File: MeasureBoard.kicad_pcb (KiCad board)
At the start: 2 copper layers, 60 x 77 mm, 129 parts, among them J1 Conn_01x04, J10 TEST_1P, J11 TEST_1P, J12 TEST_1P, J13 BARREL_JACK, J14 CONN_01X02, J15 Conn_02x05_Odd_Even, J16 Conn_01x06, J17 GS3, J18 USB_OTG, J19 Conn_01x02, J2 Conn_01x06, J20 Conn_01x02, J21 Conn_01x03, J22 Conn_01x03, J23 Conn_01x03, J24 Conn_01x03, J25 Conn_01x03, J26 Conn_01x03, J27 Conn_02x05_Odd_Even, J3 Conn_01x04, J4 GS3, J5 GS2, J6 Conn_01x04, J7 Conn_01x03, J8 Conn_01x04, J9 TEST_1P, SW1 DIP_SW_2P, SW2 SKRPACE010, SW3 SKRPACE010, SW4 SKRPACE010, U1 L7805, U2 AP1117-33, U3 STM32F103CBTx, U4 NC7SZ08, U5 SP3481CN, U6 NC7WZ241, U7 MCP2562-E-SN, U8 AM26LV32, Y1 Crystal

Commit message: USBのいち変更
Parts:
- moved R19 1.75 mm to (59.5, 93.9), turned to 0 degrees
- moved J18 1.20 mm to (54.0, 92.8)
- moved F1 0.20 mm to (61.0, 90.0)
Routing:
- net GND: track 1161.2 -> 1159.9 mm, vias 267 -> 264
- net Net-(FL1-Pad3): track 32.6 -> 31.4 mm
- net Net-(FL1-Pad1): track 33.3 -> 32.1 mm
- net Net-(F1-Pad2): track 5.19 -> 4.02 mm
- net Net-(D11-Pad2): track 4.52 -> 5.08 mm
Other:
- outline, holes or cut-outs redrawn
- board text added: "v1.1"
- board text removed: "v1.0"

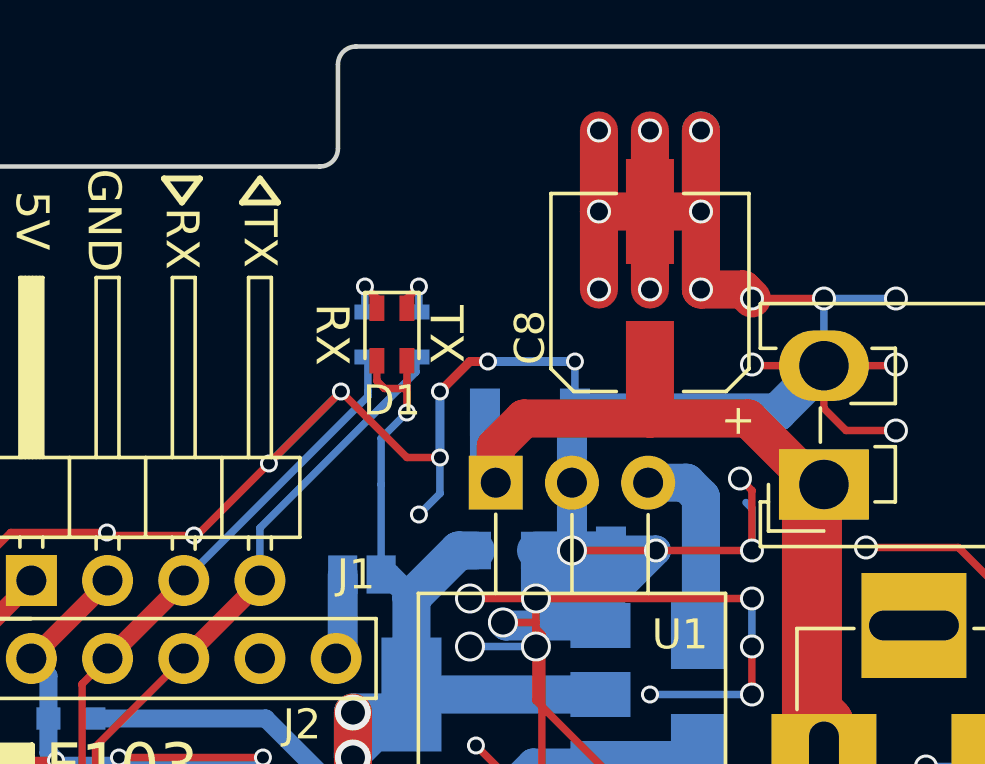
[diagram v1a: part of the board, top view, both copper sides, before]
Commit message: KiCadのバージョンを5.0にアップデート USART3のLEDを調整
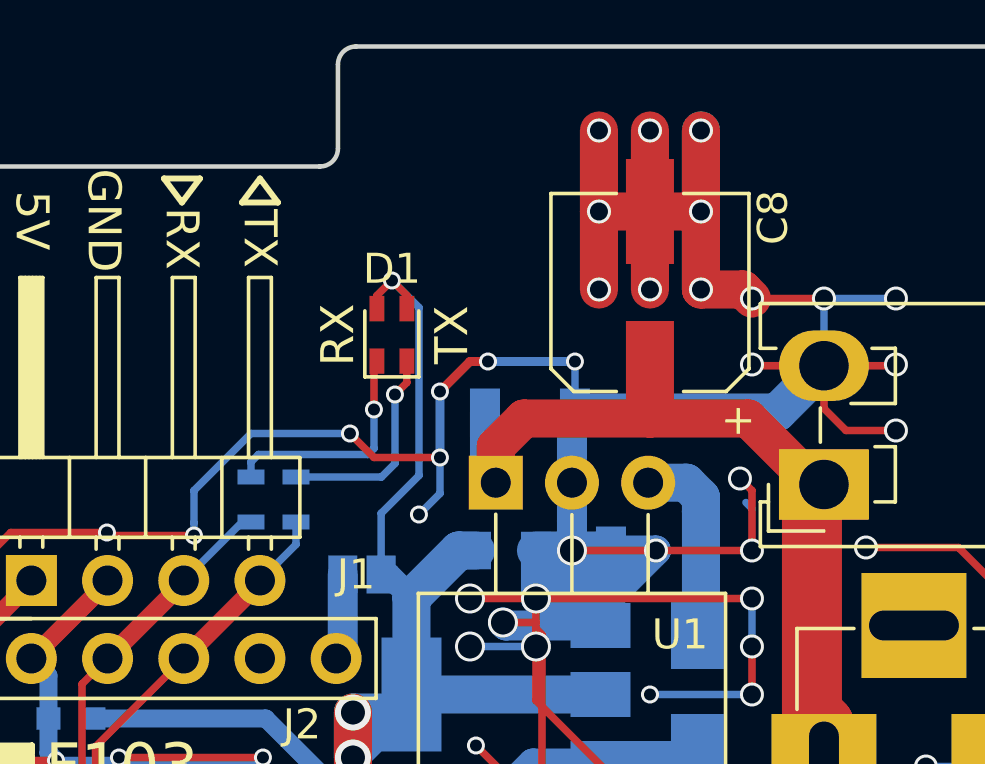
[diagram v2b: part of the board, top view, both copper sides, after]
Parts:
- moved R1 6.80 mm to (78.6, 88.1)
- moved R2 6.74 mm to (77.1, 88.1)
- turned D1 to 90 degrees
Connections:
- R1 pad 2: Net-(D1-Pad2) -> Net-(D1-Pad4)
- R2 pad 2: Net-(D1-Pad4) -> Net-(D1-Pad2)
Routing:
- net /MCU/USART1_TX: track 46.6 -> 39.5 mm
- net /MCU/USART1_RX: track 44.9 -> 38.0 mm
- net Net-(D1-Pad2): track 1.78 -> 7.74 mm
- net Net-(D1-Pad4): track 1.78 -> 7.06 mm
- net +3V3: track 299.2 -> 302.9 mm
- net GND: track 1159.9 -> 1156.4 mm, vias 264 -> 263

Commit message: アノテーションしたけど部品配置がパーになって萎えた
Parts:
- removed C39, C40: 220p, Capacitors_SMD:C_0603
- removed D12: D_TVS, Diodes_SMD:D_SOD-323
- removed J20: Conn_01x02, Pin_Headers:Pin_Header_Straight_2x01_Pitch2.54mm
- removed J21, J22, J23, J24, J25, J26: Conn_01x03, Connectors_JST:JST_EH_B03B-EH-A_03x2.50mm_Straight
- removed J27: Conn_02x05_Odd_Even, Connectors_Multicomp:Multicomp_MC9A12-1034_2x05x2.54mm_Straight
- added JP1: Jumper_2_Open, Jumper:SolderJumper-2_P1.3mm_Open_RoundedPad1.0x1.5mm, F.Cu at (178.5, 73.1)
- added JP2: SolderJumper_3_Open, Jumper:SolderJumper-3_P1.3mm_Open_RoundedPad1.0x1.5mm, F.Cu at (214.6, 84.1)
- added Q1: BSS138, Package_TO_SOT_SMD:SOT-23, F.Cu at (245.7, 84.7)
- added R29: 1.5k, Resistor_SMD:R_0603_1608Metric, F.Cu at (248.9, 85.2)
- added R30: 10k, Resistor_SMD:R_0603_1608Metric, F.Cu at (248.9, 83.7)
- added R31: 36k, Resistor_SMD:R_0603_1608Metric, F.Cu at (241.1, 86.3)
- added R32: R, Resistor_SMD:R_0603_1608Metric, F.Cu at (241.1, 84.8)
- added TP1: TestPoint, MountingHole:MountingHole_3.2mm_M3_Pad, F.Cu at (106.0, 146.0)
- added TP2: TestPoint, MountingHole:MountingHole_3.2mm_M3_Pad, F.Cu at (54.0, 77.0)
- added TP3: TestPoint, MountingHole:MountingHole_3.2mm_M3_Pad, F.Cu at (106.0, 77.0)
- added TP4: TestPoint, MountingHole:MountingHole_3.2mm_M3_Pad, F.Cu at (54.0, 146.0)
- C1, C10, C11, C12, C14, C15, C16, C17, C18, C19, C20, C21, C22, C23, C24, C25, C26, C27, C28, C29, C30, C31, C35, C36, C9: footprint Capacitors_SMD:C_0603 -> Capacitor_SMD:C_0603_1608Metric; moved to F.Cu
- C13: footprint Capacitors_SMD:C_0603 -> Capacitor_SMD:C_0603_1608Metric
- C2, C3: value 0.1u -> C; footprint Capacitors_SMD:C_0603 -> Capacitor_SMD:C_0603_1608Metric; moved to F.Cu
- C32, C33, C34: value 0.1u -> 220p; footprint Capacitors_SMD:C_0603 -> Capacitor_SMD:C_0603_1608Metric; moved to F.Cu
- C37, C38: value 220p -> 0.1u; footprint Capacitors_SMD:C_0603 -> Capacitor_SMD:C_0603_1608Metric; moved to F.Cu
- C4, C6: footprint Capacitors_SMD:C_1206 -> Capacitor_SMD:C_1206_3216Metric; moved to F.Cu
- C5, C7: footprint Capacitors_SMD:C_0805 -> Capacitor_SMD:C_0805_2012Metric; moved to F.Cu
- C8: footprint Capacitors_SMD:CP_Elec_6.3x7.7 -> Capacitor_SMD:CP_Elec_6.3x9.9
- D10: value LED -> D; footprint LEDs:LED_0603 -> Diode_SMD:D_SOD-123F
- D11: value D -> D_TVS; footprint Diodes_SMD:D_SMA -> Diode_SMD:D_SOD-323; moved to F.Cu
- D2: footprint Diodes_SMD:D_SMA -> Diode_SMD:D_SOD-123F; moved to F.Cu
- D3, D4, D5, D9: footprint LEDs:LED_0603 -> LED_SMD:LED_0603_1608Metric
- D7: value D_Zener_Small -> D; footprint Diodes_SMD:D_SOD-323 -> Diode_SMD:D_SOD-123F; moved to F.Cu
- D8: value D -> LED; footprint Diodes_SMD:D_SMA -> LED_SMD:LED_0603_1608Metric; moved to F.Cu
- F1: footprint Fuse_Holders_and_Fuses:Fuse_0679H -> Fuse:Fuse_2816_7142Metric
- J1: footprint Pin_Headers:Pin_Header_Angled_1x04_Pitch2.54mm -> Connector_PinHeader_2.54mm:PinHeader_1x04_P2.54mm_Horizontal
- J10: value TEST_1P -> Conn_01x06; footprint Mounting_Holes:MountingHole_3.2mm_M3_Pad -> Connector_JST:JST_EH_B06B-EH-A_1x06_P2.50mm_Vertical
- J11: value TEST_1P -> USB_B_Micro; footprint Mounting_Holes:MountingHole_3.2mm_M3_Pad -> Connector_USB:USB_Micro-B_Molex-105017-0001
- J12: value TEST_1P -> Conn_01x02; footprint Mounting_Holes:MountingHole_3.2mm_M3_Pad -> Connector_PinHeader_2.54mm:PinHeader_1x02_P2.54mm_Vertical
- J13: value BARREL_JACK -> Conn_01x02; footprint Connectors:BARREL_JACK -> Connector_PinHeader_2.54mm:PinHeader_1x02_P2.54mm_Vertical
- J14: value CONN_01X02 -> Conn_01x03; footprint Connectors_JST:JST_VH_S2P-VH_2x2x3.96mm_Horizontal -> Connector_JST:JST_EH_B03B-EH-A_1x03_P2.50mm_Vertical
- J15: value Conn_02x05_Odd_Even -> Conn_01x03; footprint Pin_Headers:Pin_Header_Straight_2x05_Pitch1.27mm_SMD -> Connector_JST:JST_EH_B03B-EH-A_1x03_P2.50mm_Vertical
- J16: value Conn_01x06 -> Conn_01x03; footprint Connectors_JST:JST_EH_B06B-EH-A_06x2.50mm_Straight -> Connector_JST:JST_EH_B03B-EH-A_1x03_P2.50mm_Vertical
- J17: value GS3 -> Conn_02x05_Odd_Even; footprint Connectors:GS3 -> Connector_Multicomp:Multicomp_MC9A12-1034_2x05_P2.54mm_Vertical; moved to F.Cu
- J18: value USB_OTG -> Conn_01x03; footprint Connectors:USB_Micro-B -> Connector_JST:JST_EH_B03B-EH-A_1x03_P2.50mm_Vertical
- J19: value Conn_01x02 -> Conn_01x03; footprint Pin_Headers:Pin_Header_Straight_1x02_Pitch2.54mm -> Connector_JST:JST_EH_B03B-EH-A_1x03_P2.50mm_Vertical
- J2: footprint Pin_Headers:Pin_Header_Straight_1x06_Pitch2.54mm -> Connector_PinHeader_2.54mm:PinHeader_1x06_P2.54mm_Vertical
- J3: footprint Connectors_JST:JST_EH_B04B-EH-A_04x2.50mm_Straight -> Connector_JST:JST_EH_S04B-EH_1x04_P2.50mm_Horizontal
- J4: value GS3 -> Conn_01x04; footprint Connectors:GS3 -> Connector_JST:JST_EH_B04B-EH-A_1x04_P2.50mm_Vertical; moved to F.Cu
- J5: value GS2 -> Conn_01x03; footprint Connectors:GS2 -> Connector_JST:JST_EH_S03B-EH_1x03_P2.50mm_Horizontal; moved to F.Cu
- J6: footprint Connectors_JST:JST_EH_B04B-EH-A_04x2.50mm_Straight -> Connector_JST:JST_EH_B04B-EH-A_1x04_P2.50mm_Vertical
- J7: value Conn_01x03 -> Barrel_Jack_Switch; footprint Connectors_JST:JST_EH_B03B-EH-A_03x2.50mm_Straight -> Connector_BarrelJack:BarrelJack_Horizontal
- J8: value Conn_01x04 -> Conn_01x02; footprint Connectors_JST:JST_EH_B04B-EH-A_04x2.50mm_Straight -> Connector_JST:JST_VH_B2PS-VH_1x02_P3.96mm_Horizontal
- J9: value TEST_1P -> Conn_02x05_Odd_Even; footprint Mounting_Holes:MountingHole_3.2mm_M3_Pad -> Connector_PinHeader_1.27mm:PinHeader_2x05_P1.27mm_Vertical_SMD
- L1: footprint Capacitors_SMD:C_0603 -> Inductor_SMD:L_0603_1608Metric; moved to F.Cu
- R1, R14, R15, R16, R17, R2, R20, R21, R22, R23, R24, R25, R26, R27, R28, R3, R4, R5, R8, R9: footprint Resistors_SMD:R_0603 -> Resistor_SMD:R_0603_1608Metric; moved to F.Cu
- R10, R11, R12, R13, R6, R7: value 4.7k -> 4k7; footprint Resistors_SMD:R_0603 -> Resistor_SMD:R_0603_1608Metric; moved to F.Cu
- R18: footprint Resistors_SMD:R_0603 -> Resistor_SMD:R_0603_1608Metric
- R19: value 100k -> R; footprint Resistors_SMD:R_0603 -> Resistor_SMD:R_0603_1608Metric
- RN1, RN5: value 10k_4 -> R_Pack04; footprint Resistors_SMD:R_Array_Concave_4x0603 -> Resistor_SMD:R_Array_Concave_4x0603
- RN2: value 150_4 -> R_Pack04; footprint Resistors_SMD:R_Array_Concave_4x0603 -> Resistor_SMD:R_Array_Concave_4x0603
- RN3, RN4: value 150_4 -> R_Pack04; footprint Resistors_SMD:R_Array_Concave_4x0603 -> Resistor_SMD:R_Array_Concave_4x0603; moved to F.Cu
- RN6: value 20k_4 -> R_Pack02; footprint Resistors_SMD:R_Array_Concave_4x0603 -> Resistor_SMD:R_Array_Concave_2x0603; moved to F.Cu
- SW1: footprint Buttons_Switches_THT:SW_DIP_x2_W7.62mm_Slide_LowProfile -> Button_Switch_THT:SW_DIP_SPSTx02_Slide_6.7x6.64mm_W7.62mm_P2.54mm_LowProfile
- SW2, SW3, SW4: footprint SMD_Packages:ALPS_SKRPAxE010 -> Button_Switch_SMD_my:ALPS_SKRPAxE010
- U1: footprint TO_SOT_Packages_THT:TO-220-3_Horizontal_Reversed -> Package_TO_SOT_THT:TO-220-3_Horizontal_TabUp
- U2: footprint TO_SOT_Packages_SMD:SOT-223-3_TabPin2 -> Package_TO_SOT_SMD:SOT-223-3_TabPin2; moved to F.Cu
- U3: value STM32F103CBTx -> STM32F303CCTx; footprint Housings_QFP:LQFP-48_7x7mm_Pitch0.5mm -> Package_QFP:LQFP-48_7x7mm_P0.5mm
- U4: footprint TO_SOT_Packages_SMD:SOT-23-5 -> Package_TO_SOT_SMD:SOT-23-5; moved to F.Cu
- U5, U7: footprint Housings_SOIC:SOIC-8_3.9x4.9mm_Pitch1.27mm -> Package_SO:SOIC-8_3.9x4.9mm_P1.27mm; moved to F.Cu
- U6: footprint Housings_SSOP:VSSOP-8_2.3x2mm_Pitch0.5mm -> Package_SO:VSSOP-8_2.3x2mm_P0.5mm; moved to F.Cu
- U8: footprint Housings_SOIC:SOIC-16_3.9x9.9mm_Pitch1.27mm -> Package_SO:SOIC-16_3.9x9.9mm_P1.27mm; moved to F.Cu
- Y1: footprint Crystals:NDK_Crystal_SMD_3225_2Pads -> Crystal_my:NDK_Crystal_SMD_3225_2Pads; moved to F.Cu
- moved R19 189.6 mm to (248.9, 86.7)
- moved F1 187.5 mm to (248.3, 80.4), turned to 0 degrees
- moved J16 173.4 mm to (226.3, 64.2), turned to 0 degrees
- moved D10 172.9 mm to (237.4, 85.3), turned to 0 degrees
- moved C28 172.3 mm to (219.8, 74.1), turned to 0 degrees
- moved C27 171.1 mm to (216.8, 74.1), turned to 0 degrees
- moved C26 170.1 mm to (213.8, 74.1), turned to 0 degrees
- moved FL1 169.4 mm to (236.4, 87.1), turned to 0 degrees
- moved D11 168.7 mm to (229.2, 101.1), turned to 0 degrees
- moved RN1 164.5 mm to (224.9, 68.9), turned to 0 degrees
- moved C25 158.8 mm to (219.8, 72.6), turned to 0 degrees
- moved J18 155.3 mm to (209.0, 101.8), turned to 0 degrees
- moved C23 155.0 mm to (216.8, 72.6), turned to 0 degrees
- moved C24 152.8 mm to (213.8, 72.6), turned to 0 degrees
- moved R6 150.8 mm to (207.3, 73.0), turned to 0 degrees
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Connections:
- C10 pad 1: GND -> Net-(C10-Pad1)
- C10 pad 2: Net-(C10-Pad2) -> GND
- C11 pad 1: +3V3 -> GND
- C11 pad 2: GND -> +3V3
- C14 pad 1: +3V3 -> GND
- C14 pad 2: GND -> +3V3
- C15 pad 1: +3V3 -> GND
- C15 pad 2: GND -> +3V3
- C16 pad 1: +3V3 -> GND
- C16 pad 2: GND -> +3V3
- C23 pad 2: GND -> Net-(C23-Pad2)
- C24 pad 2: GND -> Net-(C23-Pad2)
- C25 pad 2: GND -> Net-(C23-Pad2)
- C29 pad 1: /IN_Di/DI3_LPF -> Net-(C29-Pad1)
- C30 pad 1: /IN_Di/DI2_LPF -> Net-(C30-Pad1)
- C31 pad 1: /IN_Di/DI1_LPF -> Net-(C31-Pad1)
- C32 pad 1: +5V -> Net-(C32-Pad1)
- C33 pad 1: +5V -> Net-(C33-Pad1)
- C34 pad 1: +5V -> Net-(C34-Pad1)
- C35 pad 1: Net-(C35-Pad1) -> /IN_Di/DI2_LPF
- C36 pad 1: Net-(C36-Pad1) -> /IN_Di/DI1_LPF
- C37 pad 1: Net-(C37-Pad1) -> +5V
- C38 pad 1: Net-(C38-Pad1) -> +5V
- C4 pad 2: GND -> Net-(C4-Pad2)
- C6 pad 2: GND -> Net-(C4-Pad2)
- C9 pad 1: GND -> Net-(C9-Pad1)
- C9 pad 2: Net-(C9-Pad2) -> GND
- D10 pad 1: GND -> +5V
- D11 pad 1: +5V -> /RS485-TTL/TTL_DATA
- D11 pad 2: Net-(D11-Pad2) -> GND
- D7 pad 1: /IN_Di/DI3_LPF -> +5V
- D7 pad 2: GND -> Net-(C6-Pad1)
- D8 pad 1: +5V -> GND
- D8 pad 2: Net-(C6-Pad1) -> Net-(D8-Pad2)
- F1 pad 1: Net-(D11-Pad2) -> Net-(D10-Pad2)
- FL1 pad 1: Net-(FL1-Pad1) -> /USB/USB_+
- FL1 pad 2: /USB/D- -> /USB/D+
- FL1 pad 3: Net-(FL1-Pad3) -> /USB/USB_-
- FL1 pad 4: /USB/D+ -> /USB/D-
- J11 pad 1: Net-(J11-Pad1) -> Net-(F1-Pad2)
- J13 pad 1: +12V -> /CAN/CAN_H
- J13 pad 2: GND -> Net-(J13-Pad2)
- J14 pad 1: +12V -> GND
- J14 pad 2: GND -> +3V3
- J15 pad 1: +3V3 -> GND
- J15 pad 2: /JTAG/SWDIO-TMS -> +3V3
- J15 pad 3: GND -> Net-(J15-Pad3)
- J16 pad 1: Net-(J16-Pad1) -> GND
- J16 pad 2: GND -> +3V3
- J16 pad 3: /SSI/NSS -> Net-(J16-Pad3)
- J17 pad 1: +3V3 -> (no net)
- J17 pad 2: Net-(J16-Pad1) -> +5V
- J17 pad 3: +5V -> (no net)
- J18 pad 1: Net-(F1-Pad2) -> GND
- J18 pad 2: Net-(FL1-Pad1) -> +5V
- J18 pad 3: Net-(FL1-Pad3) -> Net-(J18-Pad3)
- J19 pad 1: Net-(J19-Pad1) -> GND
- J19 pad 2: /RS485-TTL/RS485_B -> +5V
- J2 pad 5: Net-(J2-Pad5) -> (no net)
- J3 pad 1: Net-(J3-Pad1) -> (no net)
- J4 pad 1: +3V3 -> GND
- J4 pad 2: Net-(J3-Pad1) -> +12V
- J4 pad 3: +5V -> /RS485-TTL/RS485_A
- J5 pad 1: +3V3 -> GND
- J5 pad 2: Net-(J2-Pad6) -> +12V
- J6 pad 3: /RS485-TTL/RS485_A -> /CAN/CAN_H
- J6 pad 4: /RS485-TTL/RS485_B -> /CAN/CAN_L
- J7 pad 1: GND -> +12V
- J7 pad 2: +12V -> GND
- J7 pad 3: /RS485-TTL/TTL_DATA -> (no net)
- J8 pad 1: GND -> +12V
- J8 pad 2: +12V -> GND
- J9 pad 1: Net-(J9-Pad1) -> +3V3
- R16 pad 1: Net-(D9-Pad2) -> +5V
- R16 pad 2: +5V -> Net-(D8-Pad2)
- R17 pad 1: Net-(D10-Pad2) -> +3V3
- R17 pad 2: +3V3 -> Net-(D9-Pad2)
- R19 pad 1: Net-(J18-Pad4) -> Net-(J11-Pad4)
- R20 pad 1: Net-(R20-Pad1) -> +3V3
- R20 pad 2: +3V3 -> Net-(R20-Pad2)
- R21 pad 1: Net-(R21-Pad1) -> +3V3
- R21 pad 2: +3V3 -> Net-(R21-Pad2)
- R22 pad 1: /RS485-TTL/RS485_A -> Net-(J12-Pad1)
- R22 pad 2: Net-(J19-Pad1) -> /RS485-TTL/RS485_A
- R23 pad 1: /RS485-TTL/TTL_DATA -> +5V
- R23 pad 2: +5V -> /RS485-TTL/TTL_DATA
- R24 pad 1: GND -> Net-(R24-Pad1)
- R24 pad 2: Net-(R24-Pad2) -> GND
- R25 pad 1: /CAN/CAN_L -> Net-(J13-Pad2)
- R25 pad 2: Net-(J20-Pad2) -> /CAN/CAN_L
- R26 pad 1: Net-(C36-Pad1) -> Net-(C30-Pad1)
- R27 pad 1: Net-(C38-Pad1) -> Net-(C32-Pad1)
- R28 pad 1: Net-(C40-Pad1) -> Net-(C34-Pad1)
- R3 pad 1: GND -> Net-(D3-Pad1)
- R3 pad 2: Net-(D3-Pad1) -> GND
- R4 pad 1: GND -> Net-(D4-Pad1)
- R4 pad 2: Net-(D4-Pad1) -> GND
- R5 pad 1: GND -> Net-(D5-Pad1)
- R5 pad 2: Net-(D5-Pad1) -> GND
- R8 pad 1: Net-(D6-Pad4) -> /RS485-TTL/DI
- R8 pad 2: /RS485-TTL/DI -> Net-(D6-Pad4)
- R9 pad 1: Net-(D6-Pad2) -> /RS485-TTL/RO
- R9 pad 2: /RS485-TTL/RO -> Net-(D6-Pad2)
- RN1 pad 4: Net-(RN1-Pad4) -> (no net)
- RN1 pad 5: Net-(RN1-Pad5) -> (no net)
- RN1 pad 6: Net-(J23-Pad3) -> Net-(J16-Pad3)
- RN1 pad 7: Net-(J22-Pad3) -> Net-(J15-Pad3)
- RN1 pad 8: Net-(J21-Pad3) -> Net-(J14-Pad3)
- RN2 pad 1: Net-(RN2-Pad1) -> Net-(J17-Pad5)
- RN2 pad 2: /IN_Di/DI3_LPF -> Net-(J17-Pad7)
- RN2 pad 3: /IN_Di/DI2_LPF -> Net-(J17-Pad9)
- RN2 pad 4: /IN_Di/DI1_LPF -> (no net)
- RN2 pad 5: Net-(J26-Pad3) -> (no net)
- RN2 pad 6: Net-(J25-Pad3) -> Net-(C34-Pad1)
- RN2 pad 7: Net-(J24-Pad3) -> Net-(C32-Pad1)
- RN2 pad 8: Net-(RN2-Pad8) -> Net-(C30-Pad1)
- RN3 pad 1: Net-(J27-Pad5) -> Net-(J17-Pad6)
- RN3 pad 2: Net-(J27-Pad7) -> Net-(J17-Pad8)
- RN3 pad 3: Net-(J27-Pad9) -> Net-(J17-Pad10)
- RN3 pad 4: Net-(RN3-Pad4) -> (no net)
- RN3 pad 5: Net-(RN3-Pad5) -> (no net)
- RN3 pad 6: Net-(C40-Pad1) -> Net-(C33-Pad1)
- RN3 pad 7: Net-(C38-Pad1) -> Net-(C31-Pad1)
- RN3 pad 8: Net-(C36-Pad1) -> Net-(C29-Pad1)
- RN4 pad 1: Net-(J27-Pad6) -> Net-(C29-Pad1)
- RN4 pad 2: Net-(J27-Pad8) -> Net-(C31-Pad1)
- RN4 pad 3: Net-(J27-Pad10) -> Net-(C33-Pad1)
- RN4 pad 4: Net-(RN4-Pad4) -> (no net)
- RN4 pad 5: Net-(RN4-Pad5) -> (no net)
- RN4 pad 6: Net-(C39-Pad1) -> +3V3
- RN4 pad 7: Net-(C37-Pad1) -> +3V3
- RN4 pad 8: Net-(C35-Pad1) -> +3V3
- RN5 pad 1: Net-(C35-Pad1) -> (no net)
- RN5 pad 2: Net-(C37-Pad1) -> Net-(C30-Pad1)
- RN5 pad 3: Net-(C39-Pad1) -> Net-(C32-Pad1)
- RN5 pad 4: Net-(RN5-Pad4) -> Net-(C34-Pad1)
- RN5 pad 5: Net-(RN5-Pad5) -> +3V3
- RN5 pad 8: +3V3 -> (no net)
- RN6 pad 1: Net-(RN6-Pad1) -> /IN_Di/DI2_LPF
- RN6 pad 2: Net-(C36-Pad1) -> /IN_Di/DI1_LPF
- RN6 pad 3: Net-(C38-Pad1) -> Net-(J19-Pad3)
- RN6 pad 4: Net-(C40-Pad1) -> Net-(J18-Pad3)
- SW2 pad 1: Net-(SW2-Pad1) -> (no net)
- SW3 pad 1: Net-(SW3-Pad1) -> (no net)
- SW4 pad 1: Net-(SW4-Pad1) -> (no net)
- SW4 pad 3: Net-(SW4-Pad3) -> (no net)
- U1 pad 2: GND -> Net-(C4-Pad2)
- U3 pad 28: /IN_Di/DI3_LPF -> /USB_EN
- U3 pad 5: Net-(C9-Pad2) -> Net-(C9-Pad1)
- U3 pad 6: Net-(C10-Pad2) -> Net-(C10-Pad1)
- U4 pad 1: Net-(R20-Pad1) -> Net-(R20-Pad2)
- U4 pad 2: Net-(R21-Pad1) -> Net-(R21-Pad2)
- U5 pad 1: Net-(R21-Pad1) -> Net-(R21-Pad2)
- U6 pad 6: Net-(R20-Pad1) -> Net-(R20-Pad2)
- U7 pad 8: Net-(R24-Pad2) -> Net-(R24-Pad1)
- U8 pad 1: Net-(C36-Pad1) -> Net-(C30-Pad1)
- U8 pad 10: Net-(C39-Pad1) -> Net-(C33-Pad1)
- U8 pad 13: Net-(U8-Pad13) -> (no net)
- U8 pad 14: Net-(U8-Pad14) -> (no net)
- U8 pad 15: Net-(U8-Pad15) -> (no net)
- U8 pad 2: Net-(C35-Pad1) -> Net-(C29-Pad1)
- U8 pad 6: Net-(C37-Pad1) -> Net-(C31-Pad1)
- U8 pad 7: Net-(C38-Pad1) -> Net-(C32-Pad1)
- U8 pad 9: Net-(C40-Pad1) -> Net-(C34-Pad1)
- Y1 pad 1: Net-(C9-Pad2) -> Net-(C9-Pad1)
- Y1 pad 2: Net-(C10-Pad2) -> Net-(C10-Pad1)
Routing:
- net GND: track 1156.4 -> 421.2 mm, vias 263 -> 113
- net (no net): track 0.00 -> 564.2 mm, vias 0 -> 114
- net Net-(C4-Pad2): track 0.00 -> 142.9 mm, vias 0 -> 31
- net Net-(FL1-Pad1): track 32.1 -> 0.00 mm
- net /USB/USB_-: track 0.00 -> 32.1 mm
- net Net-(FL1-Pad3): track 31.4 -> 14.5 mm
- net +12V: track 81.2 -> 64.5 mm
- net Net-(C10-Pad2): track 11.3 -> 0.00 mm
- net Net-(C10-Pad1): track 0.00 -> 11.3 mm
- net Net-(C9-Pad2): track 10.1 -> 0.00 mm
- net Net-(C9-Pad1): track 0.00 -> 10.1 mm
- net Net-(J27-Pad6): track 7.94 -> 0.00 mm
- net Net-(J17-Pad6): track 0.00 -> 7.94 mm
- net Net-(J27-Pad8): track 7.46 -> 0.00 mm
- net Net-(J17-Pad8): track 0.00 -> 7.46 mm
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
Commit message: AW
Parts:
- C1, C10, C11, C12, C14, C15, C16, C17, C18, C19, C2, C20, C21, C22, C23, C24, C25, C26, C27, C28, C29, C3, C30, C31, C32, C33, C34, C35, C36, C37, C38, C4, C5, C6, C7, C9, D10, D11, D2, D7, JP1, JP2, L1, Q1, R1, R10, R11, R12, R13, R14, R15, R2, R20, R21, R22, R23, R24, R25, R26, R27, R28, R29, R3, R30, R31, R32, R4, R5, R6, R7, R8, R9, RN2, RN3, RN5, U2, U4, U5, U6, U7, U8, Y1: moved to B.Cu
- J3: footprint Connector_JST:JST_EH_S04B-EH_1x04_P2.50mm_Horizontal -> Connector_JST:JST_EH_B04B-EH-A_1x04_P2.50mm_Vertical
- J5: footprint Connector_JST:JST_EH_S03B-EH_1x03_P2.50mm_Horizontal -> Connector_JST:JST_EH_B03B-EH-A_1x03_P2.50mm_Vertical
- moved R19 190.6 mm to (58.5, 95.0), turned to 270 degrees
- moved F1 187.4 mm to (61.1, 88.9), turned to 180 degrees
- moved J16 183.5 mm to (54.5, 128.5)
- moved R29 181.0 mm to (69.6, 109.9), turned to 270 degrees
- moved R30 179.5 mm to (70.7, 104.7), turned to 270 degrees
- moved J14 177.1 mm to (54.5, 138.5)
- moved FL1 177.1 mm to (59.4, 92.5)
- moved C28 175.7 mm to (55.6, 136.5), turned to 180 degrees
- moved Q1 175.4 mm to (72.1, 110.0)
- moved R32 174.4 mm to (68.9, 112.5)
- moved J15 173.2 mm to (54.5, 133.5)
- moved D10 172.9 mm to (64.9, 96.8), turned to 90 degrees
- moved R31 171.2 mm to (71.9, 112.5)
- moved C27 171.1 mm to (55.6, 131.5), turned to 180 degrees
- moved C26 166.6 mm to (55.6, 126.5), turned to 180 degrees
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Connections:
- FL1 pad 1: /USB/USB_+ -> /USB/USB_-
- FL1 pad 2: /USB/D+ -> /USB/D-
- FL1 pad 3: /USB/USB_- -> /USB/USB_+
- FL1 pad 4: /USB/D- -> /USB/D+
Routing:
- net (no net): track 564.2 -> 423.6 mm, vias 114 -> 86
- net GND: track 421.2 -> 387.0 mm, vias 113 -> 91
- net /USB/D+: track 7.68 -> 37.4 mm, vias 1 -> 2
- net /USB/D-: track 8.24 -> 37.5 mm
- net /USB/USB_-: track 32.1 -> 3.48 mm
- net Net-(C34-Pad1): track 0.00 -> 24.0 mm, vias 0 -> 2
- net Net-(C40-Pad1): track 23.3 -> 0.00 mm, vias 2 -> 0
- net Net-(C35-Pad1): track 22.8 -> 0.00 mm, vias 2 -> 0
- net Net-(C29-Pad1): track 0.00 -> 22.8 mm, vias 0 -> 2
- net Net-(C39-Pad1): track 19.4 -> 0.00 mm, vias 2 -> 0
- net Net-(C33-Pad1): track 0.00 -> 19.4 mm, vias 0 -> 2
- net Net-(C32-Pad1): track 0.00 -> 18.1 mm, vias 0 -> 3
- net Net-(C37-Pad1): track 18.0 -> 0.00 mm, vias 2 -> 0
- net Net-(C31-Pad1): track 0.00 -> 18.0 mm, vias 0 -> 2
- net Net-(C38-Pad1): track 17.6 -> 0.00 mm, vias 3 -> 0
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
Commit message: DRCパス
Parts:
- added JP3: Jumper_NC_Dual, Jumper:SolderJumper-3_P1.3mm_Open_RoundedPad1.0x1.5mm, B.Cu at (51.8, 104.2)
- F1: footprint Fuse:Fuse_2816_7142Metric -> Fuse:Fuse_1206_3216Metric
- moved D9 56.4 mm to (85.9, 111.9), turned to 90 degrees
- moved R17 33.7 mm to (85.1, 109.5)
- moved D8 31.1 mm to (95.2, 104.7), turned to 180 degrees
- moved R16 30.9 mm to (95.2, 103.1), turned to 180 degrees
- moved C8 2.78 mm to (88.0, 82.6), turned to 0 degrees
- moved F1 2.40 mm to (59.4, 90.6)
- moved C7 1.58 mm to (84.0, 89.8)
- moved J8 1.40 mm to (94.8, 87.6)
- turned C37 to 180 degrees
- turned C38 to 180 degrees
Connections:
- C23 pad 2: Net-(C23-Pad2) -> GND
- C24 pad 2: Net-(C23-Pad2) -> GND
- C25 pad 2: Net-(C23-Pad2) -> GND
- C4 pad 2: Net-(C4-Pad2) -> GND
- C6 pad 2: Net-(C4-Pad2) -> GND
- J17 pad 3: (no net) -> GND
- J3 pad 1: (no net) -> Net-(J3-Pad1)
- U1 pad 2: Net-(C4-Pad2) -> GND
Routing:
- net (no net): track 423.6 -> 0.00 mm, vias 86 -> 0
- net GND: track 387.0 -> 544.9 mm, vias 91 -> 130
- net Net-(C4-Pad2): track 142.9 -> 0.00 mm, vias 31 -> 0
- net Net-(D10-Pad2): track 0.00 -> 25.4 mm, vias 0 -> 3
- net +12V: track 66.7 -> 81.7 mm, vias 1 -> 0
- net +5V: track 183.9 -> 169.6 mm
- net Net-(F1-Pad2): track 0.00 -> 3.27 mm
- net Net-(J3-Pad1): track 0.00 -> 2.99 mm
- net Net-(D11-Pad2): track 2.59 -> 0.00 mm
- net Net-(D2-Pad2): track 3.35 -> 5.73 mm
- net +3V3: track 304.0 -> 305.9 mm
- net /RS485-TTL/DI: track 32.7 -> 34.5 mm
- net Net-(D8-Pad2): track 0.00 -> 1.60 mm
- net /MCU/USART1_TX: track 39.5 -> 38.1 mm
- net Net-(C29-Pad1): track 22.8 -> 23.6 mm
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
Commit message: ちびちび修正
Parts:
- moved C26 3.06 mm to (56.2, 123.5)
- moved J16 3.00 mm to (54.5, 125.5)
- moved C37 2.09 mm to (56.2, 116.0)
- moved J18 2.00 mm to (54.5, 118.0)
- moved C27 1.62 mm to (56.2, 130.0)
- moved J15 1.50 mm to (54.5, 132.0)
- moved R19 1.20 mm to (59.4, 94.2), turned to 0 degrees
- moved C38 0.78 mm to (56.2, 109.5)
- moved C28 0.60 mm to (56.2, 136.5)
- moved J19 0.50 mm to (54.5, 111.5)
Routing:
- net GND: track 544.9 -> 459.9 mm, vias 130 -> 105
- net Net-(J16-Pad3): track 14.6 -> 17.4 mm
- net +3V3: track 305.9 -> 304.0 mm
- net Net-(J18-Pad3): track 12.0 -> 10.2 mm
- net +5V: track 169.6 -> 168.9 mm
- net Net-(J14-Pad3): track 16.6 -> 17.2 mm
- net Net-(J15-Pad3): track 13.1 -> 12.6 mm
